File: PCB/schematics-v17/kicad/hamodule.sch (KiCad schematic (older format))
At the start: 80 parts, among them J1 2604-1104, J10 EspSense, J11 Conn_01x02_Male, J12 NoCon, J2 2604-1102, J3 USB_B_Micro, J4 ESP Relays, J5 Current Jumper, J6 GND 3.3V, J7 Conn_01x02, J8 Current Jumper, J9 2604-1104, K1 PCN-105D, K2 PCN-105D, K3 PCN-105D, K4 PCN-105D, Q1 SS8050, Q2 SS8050, SW1 EN, SW2 IO0, U1 ULN2003A, U2 ESP32-WROOM-32E, U4 LD1117AV33_TO220, U5 MCP9700T-ETT, U6 LDA210-PDIP, U7 LDA210-PDIP, U8 CP2102N-A01-GQFN28

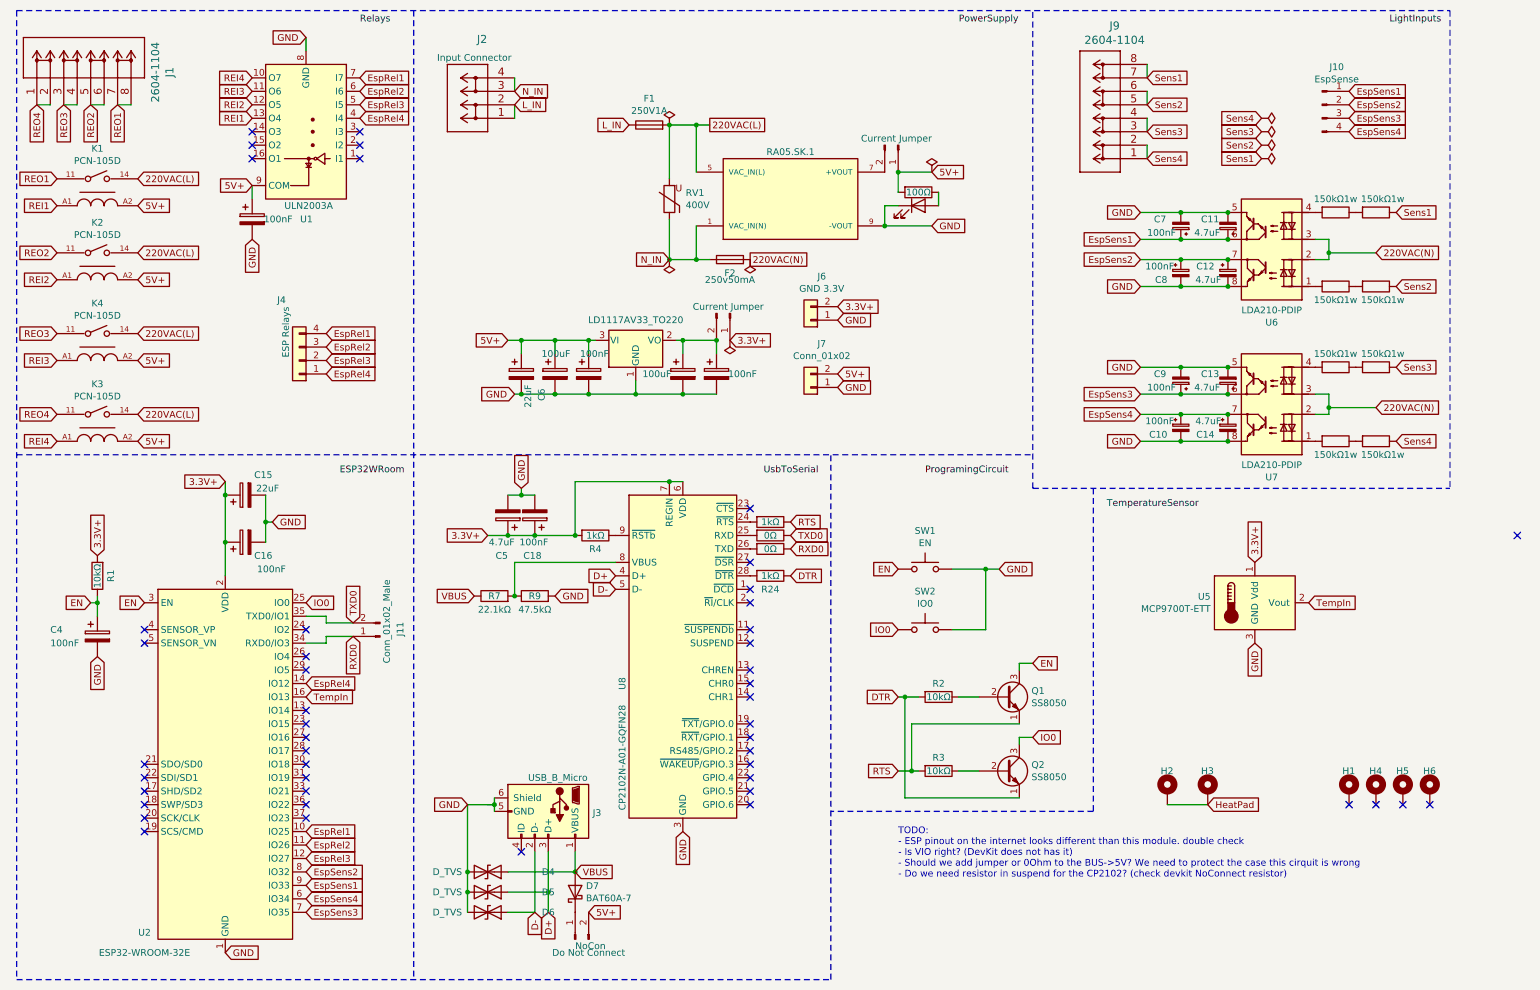
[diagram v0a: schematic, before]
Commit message: temp sensor caps + disconnect shield
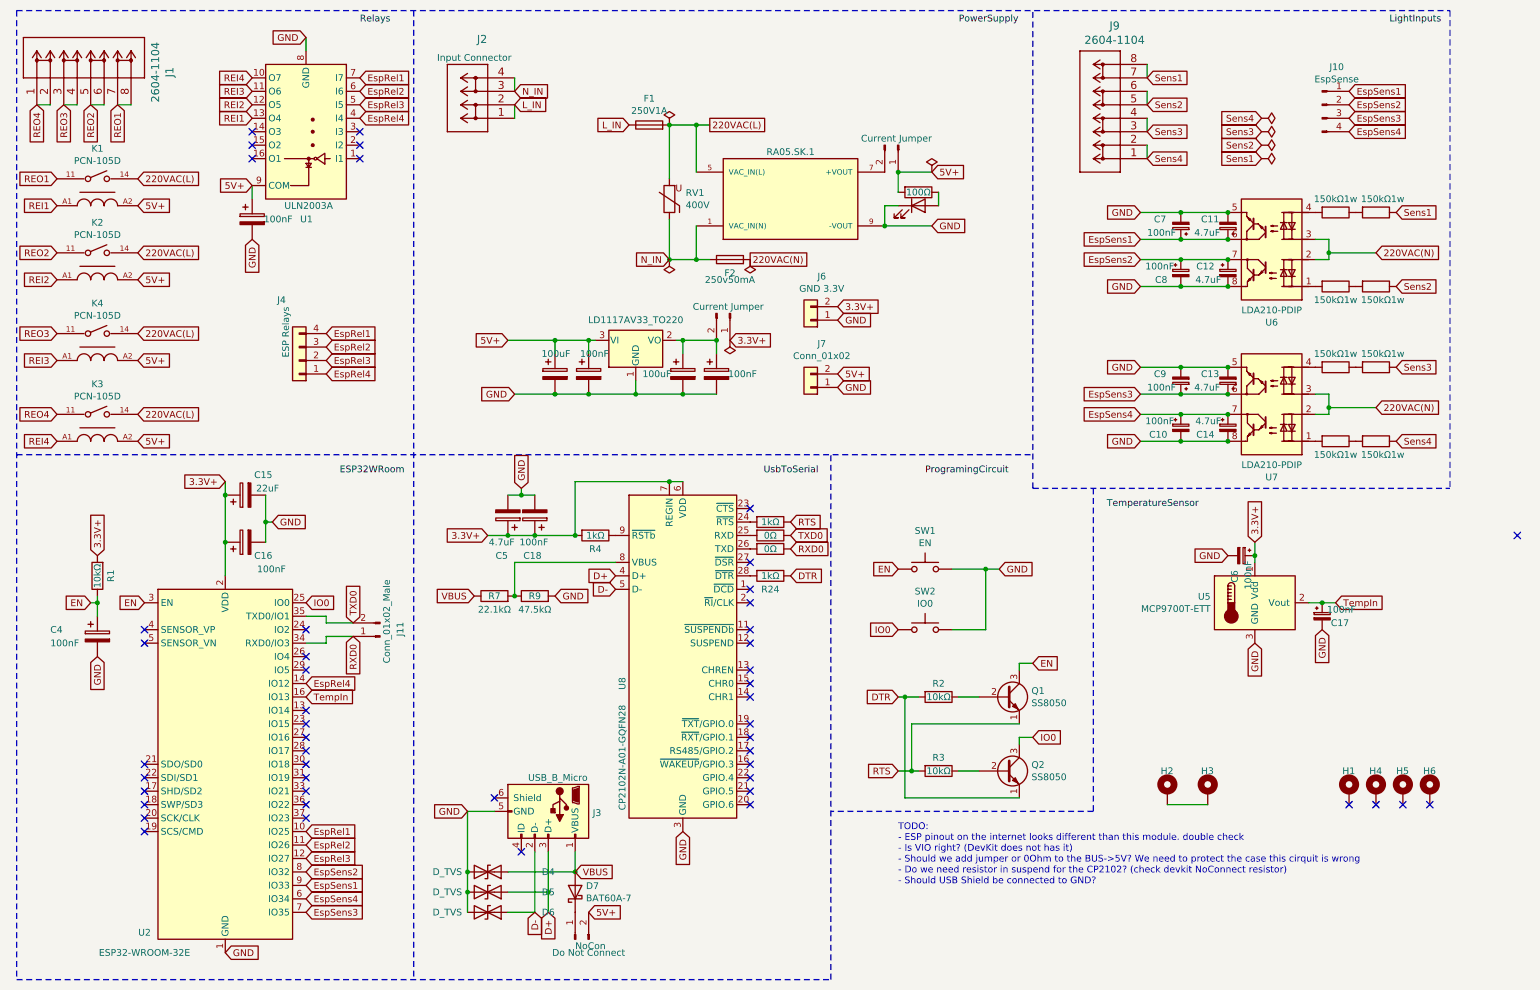
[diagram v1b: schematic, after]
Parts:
- removed C6: 22uF, Capacitor_SMD:C_0603_1608Metric_Pad1.08x0.95mm_HandSolder, symbol Device:CP
- added C17, C6: 100nF, Capacitor_SMD:C_0603_1608Metric_Pad1.08x0.95mm_HandSolder, symbol Device:CP_Small
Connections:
- net 3.3V+: now also C6.1
- net GND: now also C17.2, C6.2; no longer J3.6 (Shield)
- net TempIn: now also C17.1
- net HeatPad: no longer names the net of H2.1, H3.1
- no-connect marks 48 -> 49
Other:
- note added: "TODO:\n- ESP pinout on the internet looks different than this module. double check\n- Is VIO right? (DevKit does not has it)\n- Should we add jumper or 0Ohm to the BUS->5V? We need to protect the case this cirquit is wrong\n- Do we need resistor in suspend for the CP2102? (check devkit NoConnect resistor)\n- Should USB Shield be connected to GND?"
- note removed: "TODO:\n- ESP pinout on the internet looks different than this module. double check\n- Is VIO right? (DevKit does not has it)\n- Should we add jumper or 0Ohm to the BUS->5V? We need to protect the case this cirquit is wrong\n- Do we need resistor in suspend for the CP2102? (check devkit NoConnect resistor)"
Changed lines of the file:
@@
 NoConn ~ 5950 5650
 NoConn ~ 5950 5850
-Wire Wire Line
-	4050 6400 4050 6450
-Connection ~ 4050 6450
-Wire Wire Line
-	4050 6450 4050 6500
 Text GLabel 4450 7250 3    50   Input ~ 0
 D+
@@
 Wire Wire Line
 	3850 7250 3850 7100
-Connection ~ 3850 6950
-Wire Wire Line
-	3850 6950 3850 6450
 Connection ~ 3850 7100
 Wire Wire Line
@@
 Text GLabel 1100 4600 1    50   Input ~ 0
 3.3V+
-Text GLabel 3850 6450 0    50   Input ~ 0
+Text GLabel 3850 6500 0    50   Input ~ 0
 GND
 Text GLabel 7800 4700 2    50   Input ~ 0
@@
 Text GLabel 3900 4900 0    50   Input ~ 0
 VBUS
-Text Notes 7050 7000 0    50   ~ 0
-TODO:\n- ESP pinout on the internet looks different than this module. double check\n- Is VIO right? (DevKit does not has it)\n- Should we add jumper or 0Ohm to the BUS->5V? We need to protect the case this cirquit is wrong\n- Do we need resistor in suspend for the CP2102? (check devkit NoConnect resistor)
 Text GLabel 4650 6950 2    50   Input ~ 0
 VBUS
@@
 Text GLabel 2650 5650 2    50   Input ~ 0
 TempIn
-Text GLabel 10100 4950 2    50   Input ~ 0
+Text GLabel 10300 4950 2    50   Input ~ 0
 TempIn
 Text GLabel 9700 5250 3    50   Input ~ 0
 GND
-Text GLabel 9700 4650 1    50   Input ~ 0
+Text GLabel 9700 4500 1    50   Input ~ 0
 3.3V+
 Wire Notes Line
@@
 Connection ~ 4650 4450
 Connection ~ 4350 4450
-Text GLabel 9350 6450 2    50   Input ~ 0
-HeatPad
 Wire Wire Line
 	9350 6450 9050 6450
@@
 Connection ~ 9500 2250
 Connection ~ 9500 2050
-Wire Wire Line
-	4150 3000 4250 3000
-Wire Wire Line
-	4200 3400 4250 3400
-$Comp
-L Device:CP C6
-U 1 1 61E95A47
-P 4250 3250
-F 0 "C6" V 4400 3050 50  0000 L CNN
-F 1 "22uF" V 4300 3000 50  0000 L CNN
-F 2 "Capacitor_SMD:C_0603_1608Metric_Pad1.08x0.95mm_HandSolder" H 4288 3100 50  0001 C CNN
-F 3 "CL10A226MQ8NRNC" H 4250 3250 50  0001 C CNN
-F 4 "C59461" H 4250 3250 50  0001 C CNN "JLCPCB"
-	1    4250 3250
-	1    0    0    -1
-$EndComp
-Connection ~ 4250 3400
-Wire Wire Line
-	4250 3400 4500 3400
-Wire Wire Line
-	4250 3100 4250 3000
-Connection ~ 4250 3000
-Wire Wire Line
-	4250 3000 4500 3000
 $Comp
 L Connector:Conn_01x02_Male J12
@@
 $EndComp
 Wire Wire Line
-	4000 6450 4050 6450
-Wire Wire Line
-	3850 6450 4050 6450
+	4200 3400 4500 3400
+Wire Wire Line
+	4150 3000 4500 3000
+Wire Wire Line
+	4050 6500 3850 6500
+Wire Wire Line
+	3850 6500 3850 6950
+Connection ~ 3850 6950
+Text Notes 7050 7050 0    50   ~ 0
+TODO:\n- ESP pinout on the internet looks different than this module. double check\n- Is VIO right? (DevKit does not has it)\n- Should we add jumper or 0Ohm to the BUS->5V? We need to protect the case this cirquit is wrong\n- Do we need resistor in suspend for the CP2102? (check devkit NoConnect resistor)\n- Should USB Shield be connected to GND?
+NoConn ~ 4050 6400
+$Comp
+L Device:CP_Small C6
+U 1 1 61EA135E
+P 9600 4600
+F 0 "C6" H 9800 4550 50  0000 R CNN
+F 1 "100nF" H 9850 4650 50  0000 R CNN
+F 2 "Capacitor_SMD:C_0603_1608Metric_Pad1.08x0.95mm_HandSolder" H 9600 4600 50  0001 C CNN
+F 3 "https://www.distrelec.ch/en/ceramic-capacitor-100nf-50vdc-0805-rnd-components-rnd-1500805b104j500nt/p/30086635?q=smd+capacitor+&pos=5&origPos=990&origPageSize=50&track=true" H 9600 4600 50  0001 C CNN
+F 4 "C14663" H 9600 4600 50  0001 C CNN "JLCPCB"
+	1    9600 4600
+	0    1    1    0
+$EndComp
+$Comp
+L Device:CP_Small C17
+U 1 1 61EA5E07
+P 10200 5050
+F 0 "C17" H 10400 5000 50  0000 R CNN
+F 1 "100nF" H 10450 5100 50  0000 R CNN
+F 2 "Capacitor_SMD:C_0603_1608Metric_Pad1.08x0.95mm_HandSolder" H 10200 5050 50  0001 C CNN
+F 3 "https://www.distrelec.ch/en/ceramic-capacitor-100nf-50vdc-0805-rnd-components-rnd-1500805b104j500nt/p/30086635?q=smd+capacitor+&pos=5&origPos=990&origPageSize=50&track=true" H 10200 5050 50  0001 C CNN
+F 4 "C14663" H 10200 5050 50  0001 C CNN "JLCPCB"
+	1    10200 5050
+	1    0    0    -1
+$EndComp
+Wire Wire Line
+	10300 4950 10200 4950
+Connection ~ 10200 4950
+Wire Wire Line
+	10200 4950 10100 4950
+Wire Wire Line
+	9700 4500 9700 4600
+Connection ~ 9700 4600
+Wire Wire Line
+	9700 4600 9700 4650
+Text GLabel 10200 5150 3    50   Input ~ 0
+GND
+Text GLabel 9500 4600 0    50   Input ~ 0
+GND
 $EndSCHEMATC
